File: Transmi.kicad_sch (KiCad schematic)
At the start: 47 parts, among them J101 Bat, J104 Ant, J105 Boot, Q101 Si2301CDS, Q102 XC6220B331MR-G, SW129 SK-3296S-01-L3, U1 ESP32-S2FH4, U103 TP4056, X101 S2240000101050JY, X102 Q13FC1350000400

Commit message: Added LEDs
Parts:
- added C1, C10, C100, C102, C104, C11, C116, C117, C12, C122, C123, C124, C125, C126, C127, C128, C129, C13, C130, C131, C132, C133, C134, C135, C136, C137, C138, C139, C14, C140, C141, C142, C143, C144, C145, C146, C147, C148, C149, C15, C150, C151, C152, C153, C154, C155, C156, C157, C158, C159, C16, C160, C161, C17, C18, C19, C2, C20, C21, C22, C23, C24, C25, C26, C27, C28, C29, C3, C30, C31, C32, C33, C34, C35, C36, C37, C38, C39, C4, C40, C41, C42, C43, C44, C45, C46, C47, C48, C49, C5, C50, C51, C52, C53, C54, C55, C56, C57, C58, C59, C6, C60, C61, C62, C63, C64, C65, C66, C67, C68, C69, C7, C70, C71, C72, C73, C74, C75, C76, C77, C78, C79, C8, C80, C81, C82, C83, C84, C85, C86, C87, C88, C89, C9, C90, C91, C92, C93, C94, C95, C96, C97, C98, C99: 100n, Capacitor_SMD:C_0402_1005Metric, symbol Device:C
- added LED1, LED10, LED100, LED101, LED102, LED103, LED104, LED105, LED106, LED107, LED108, LED109, LED11, LED110, LED111, LED112, LED113, LED114, LED115, LED116, LED117, LED118, LED119, LED12, LED120, LED121, LED122, LED123, LED124, LED125, LED126, LED127, LED128, LED129, LED13, LED130, LED131, LED132, LED133, LED134, LED135, LED136, LED137, LED138, LED139, LED14, LED140, LED141, LED142, LED143, LED144, LED15, LED16, LED17, LED18, LED19, LED2, LED20, LED21, LED22, LED23, LED24, LED25, LED26, LED27, LED28, LED29, LED3, LED30, LED31, LED32, LED33, LED34, LED35, LED36, LED37, LED38, LED39, LED4, LED40, LED41, LED42, LED43, LED44, LED45, LED46, LED47, LED48, LED49, LED5, LED50, LED51, LED52, LED53, LED54, LED55, LED56, LED57, LED58, LED59, LED6, LED60, LED61, LED62, LED63, LED64, LED65, LED66, LED67, LED68, LED69, LED7, LED70, LED71, LED72, LED73, LED74, LED75, LED76, LED77, LED78, LED79, LED8, LED80, LED81, LED82, LED83, LED84, LED85, LED86, LED87, LED88, LED89, LED9, LED90, LED91, LED92, LED93, LED94, LED95, LED96, LED97, LED98, LED99: WS2812B-2020, TransmiLib:LED-SMD_4P-L2.0-W2.0-TL_WS2812B-2020, symbol TransmiLib:WS2812B-2020
- J104: footprint easyeda2kicad:ESPRESSIF_ESP32_MIFA_2.4GHz_Right -> TransmiLib:ESPRESSIF_ESP32_MIFA_2.4GHz_Right
- Q102: footprint easyeda2kicad:SOT-25-5_L3.0-W1.8-P0.95-LS3.0-BR -> TransmiLib:SOT-25_L3.0-W1.6-P0.95-LS2.8-TL; symbol easyeda2kicad:XC6220B331MR-G -> TransmiLib:XC6220B331MR-G
- SW129: footprint easyeda2kicad:SW-SMD_SK-3296S-01-L3 -> TransmiLib:SW-SMD_SK-3296S-01-L3; symbol easyeda2kicad:SK-3296S-01-L3 -> TransmiLib:SK-3296S-01-L3
- U103: footprint easyeda2kicad:ESOP-8_L4.9-W3.9-P1.27-LS6.0-BL-EP -> TransmiLib:ESOP-8_L4.9-W3.9-P1.27-LS6.0-BL-EP; symbol easyeda2kicad:TP4056 -> TransmiLib:TP4056_C725790; LCSC Part C16581 -> C725790
- USB101: footprint easyeda2kicad:USB-C-SMD_TYPE-C16PIN_C668624 -> TransmiLib:USB-C-SMD_TYPE-C16PIN_C668624; symbol easyeda2kicad:TYPE-C16P(073) -> TransmiLib:TYPE-C16P(073)
- X101: footprint easyeda2kicad:CRYSTAL-SMD_4P-L2.5-W2.0-BL -> TransmiLib:CRYSTAL-SMD_4P-L2.5-W2.0-BL; symbol easyeda2kicad:S2240000101050JY -> TransmiLib:S2240000101050; LCSC Part C555614 -> C426970
- X102: footprint easyeda2kicad:FC-135R_L3.2-W1.5 -> TransmiLib:FC-135R_L3.2-W1.5; symbol easyeda2kicad:Q13FC1350000400 -> TransmiLib:Q13FC1350000400
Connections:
- net +5V: now also C1.2, C10.2, C100.2, C102.2, C104.2, C11.2, C116.2, C117.2, C12.2, C122.2, C123.2, C124.2, C125.2, C126.2, C127.2, C128.2, C129.2, C13.2, C130.2, C131.2, C132.2, C133.2, C134.2, C135.2, C136.2, C137.2, C138.2, C139.2, C14.2, C140.2, C141.2, C142.2, C143.2, C144.2, C145.2, C146.2, C147.2, C148.2, C149.2, C15.2, C150.2, C151.2, C152.2, C153.2, C154.2, C155.2, C156.2, C157.2, C158.2, C159.2, C16.2, C160.2, C161.2, C17.2, C18.2, C19.2, C2.2, C20.2, C21.2, C22.2, C23.2, C24.2, C25.2, C26.2, C27.2, C28.2, C29.2, C3.2, C30.2, C31.2, C32.2, C33.2, C34.2, C35.2, C36.2, C37.2, C38.2, C39.2, C4.2, C40.2, C41.2, C42.2, C43.2, C44.2, C45.2, C46.2, C47.2, C48.2, C49.2, C5.2, C50.2, C51.2, C52.2, C53.2, C54.2, C55.2, C56.2, C57.2, C58.2, C59.2, C6.2, C60.2, C61.2, C62.2, C63.2, C64.2, C65.2, C66.2, C67.2, C68.2, C69.2, C7.2, C70.2, C71.2, C72.2, C73.2, C74.2, C75.2, C76.2, C77.2, C78.2, C79.2, C8.2, C80.2, C81.2, C82.2, C83.2, C84.2, C85.2, C86.2, C87.2, C88.2, C89.2, C9.2, C90.2, C91.2, C92.2, C93.2, C94.2, C95.2, C96.2, C97.2, C98.2, C99.2, LED1.4 (VDD), LED10.4 (VDD), LED100.4 (VDD), LED101.4 (VDD), LED102.4 (VDD), LED103.4 (VDD), LED104.4 (VDD), LED105.4 (VDD), LED106.4 (VDD), LED107.4 (VDD), LED108.4 (VDD), LED109.4 (VDD), LED11.4 (VDD), LED110.4 (VDD), LED111.4 (VDD), LED112.4 (VDD), LED113.4 (VDD), LED114.4 (VDD), LED115.4 (VDD), LED116.4 (VDD), LED117.4 (VDD), LED118.4 (VDD), LED119.4 (VDD), LED12.4 (VDD), LED120.4 (VDD), LED121.4 (VDD), LED122.4 (VDD), LED123.4 (VDD), LED124.4 (VDD), LED125.4 (VDD), LED126.4 (VDD), LED127.4 (VDD), LED128.4 (VDD), LED129.4 (VDD), LED13.4 (VDD), LED130.4 (VDD), LED131.4 (VDD), LED132.4 (VDD), LED133.4 (VDD), LED134.4 (VDD), LED135.4 (VDD), LED136.4 (VDD), LED137.4 (VDD), LED138.4 (VDD), LED139.4 (VDD), LED14.4 (VDD), LED140.4 (VDD), LED141.4 (VDD), LED142.4 (VDD), LED143.4 (VDD), LED144.4 (VDD), LED15.4 (VDD), LED16.4 (VDD), LED17.4 (VDD), LED18.4 (VDD), LED19.4 (VDD), LED2.4 (VDD), LED20.4 (VDD), LED21.4 (VDD), LED22.4 (VDD), LED23.4 (VDD), LED24.4 (VDD), LED25.4 (VDD), LED26.4 (VDD), LED27.4 (VDD), LED28.4 (VDD), LED29.4 (VDD), LED3.4 (VDD), LED30.4 (VDD), LED31.4 (VDD), LED32.4 (VDD), LED33.4 (VDD), LED34.4 (VDD), LED35.4 (VDD), LED36.4 (VDD), LED37.4 (VDD), LED38.4 (VDD), LED39.4 (VDD), LED4.4 (VDD), LED40.4 (VDD), LED41.4 (VDD), LED42.4 (VDD), LED43.4 (VDD), LED44.4 (VDD), LED45.4 (VDD), LED46.4 (VDD), LED47.4 (VDD), LED48.4 (VDD), LED49.4 (VDD), LED5.4 (VDD), LED50.4 (VDD), LED51.4 (VDD), LED52.4 (VDD), LED53.4 (VDD), LED54.4 (VDD), LED55.4 (VDD), LED56.4 (VDD), LED57.4 (VDD), LED58.4 (VDD), LED59.4 (VDD), LED6.4 (VDD), LED60.4 (VDD), LED61.4 (VDD), LED62.4 (VDD), LED63.4 (VDD), LED64.4 (VDD), LED65.4 (VDD), LED66.4 (VDD), LED67.4 (VDD), LED68.4 (VDD), LED69.4 (VDD), LED7.4 (VDD), LED70.4 (VDD), LED71.4 (VDD), LED72.4 (VDD), LED73.4 (VDD), LED74.4 (VDD), LED75.4 (VDD), LED76.4 (VDD), LED77.4 (VDD), LED78.4 (VDD), LED79.4 (VDD), LED8.4 (VDD), LED80.4 (VDD), LED81.4 (VDD), LED82.4 (VDD), LED83.4 (VDD), LED84.4 (VDD), LED85.4 (VDD), LED86.4 (VDD), LED87.4 (VDD), LED88.4 (VDD), LED89.4 (VDD), LED9.4 (VDD), LED90.4 (VDD), LED91.4 (VDD), LED92.4 (VDD), LED93.4 (VDD), LED94.4 (VDD), LED95.4 (VDD), LED96.4 (VDD), LED97.4 (VDD), LED98.4 (VDD), LED99.4 (VDD); no longer U103.4 (VCC)
- net +BATT: no longer U103.5 (BAT)
- net Earth: now also C1.1, C10.1, C100.1, C102.1, C104.1, C11.1, C116.1, C117.1, C12.1, C122.1, C123.1, C124.1, C125.1, C126.1, C127.1, C128.1, C129.1, C13.1, C130.1, C131.1, C132.1, C133.1, C134.1, C135.1, C136.1, C137.1, C138.1, C139.1, C14.1, C140.1, C141.1, C142.1, C143.1, C144.1, C145.1, C146.1, C147.1, C148.1, C149.1, C15.1, C150.1, C151.1, C152.1, C153.1, C154.1, C155.1, C156.1, C157.1, C158.1, C159.1, C16.1, C160.1, C161.1, C17.1, C18.1, C19.1, C2.1, C20.1, C21.1, C22.1, C23.1, C24.1, C25.1, C26.1, C27.1, C28.1, C29.1, C3.1, C30.1, C31.1, C32.1, C33.1, C34.1, C35.1, C36.1, C37.1, C38.1, C39.1, C4.1, C40.1, C41.1, C42.1, C43.1, C44.1, C45.1, C46.1, C47.1, C48.1, C49.1, C5.1, C50.1, C51.1, C52.1, C53.1, C54.1, C55.1, C56.1, C57.1, C58.1, C59.1, C6.1, C60.1, C61.1, C62.1, C63.1, C64.1, C65.1, C66.1, C67.1, C68.1, C69.1, C7.1, C70.1, C71.1, C72.1, C73.1, C74.1, C75.1, C76.1, C77.1, C78.1, C79.1, C8.1, C80.1, C81.1, C82.1, C83.1, C84.1, C85.1, C86.1, C87.1, C88.1, C89.1, C9.1, C90.1, C91.1, C92.1, C93.1, C94.1, C95.1, C96.1, C97.1, C98.1, C99.1, LED1.2 (GND), LED10.2 (GND), LED100.2 (GND), LED101.2 (GND), LED102.2 (GND), LED103.2 (GND), LED104.2 (GND), LED105.2 (GND), LED106.2 (GND), LED107.2 (GND), LED108.2 (GND), LED109.2 (GND), LED11.2 (GND), LED110.2 (GND), LED111.2 (GND), LED112.2 (GND), LED113.2 (GND), LED114.2 (GND), LED115.2 (GND), LED116.2 (GND), LED117.2 (GND), LED118.2 (GND), LED119.2 (GND), LED12.2 (GND), LED120.2 (GND), LED121.2 (GND), LED122.2 (GND), LED123.2 (GND), LED124.2 (GND), LED125.2 (GND), LED126.2 (GND), LED127.2 (GND), LED128.2 (GND), LED129.2 (GND), LED13.2 (GND), LED130.2 (GND), LED131.2 (GND), LED132.2 (GND), LED133.2 (GND), LED134.2 (GND), LED135.2 (GND), LED136.2 (GND), LED137.2 (GND), LED138.2 (GND), LED139.2 (GND), LED14.2 (GND), LED140.2 (GND), LED141.2 (GND), LED142.2 (GND), LED143.2 (GND), LED144.2 (GND), LED15.2 (GND), LED16.2 (GND), LED17.2 (GND), LED18.2 (GND), LED19.2 (GND), LED2.2 (GND), LED20.2 (GND), LED21.2 (GND), LED22.2 (GND), LED23.2 (GND), LED24.2 (GND), LED25.2 (GND), LED26.2 (GND), LED27.2 (GND), LED28.2 (GND), LED29.2 (GND), LED3.2 (GND), LED30.2 (GND), LED31.2 (GND), LED32.2 (GND), LED33.2 (GND), LED34.2 (GND), LED35.2 (GND), LED36.2 (GND), LED37.2 (GND), LED38.2 (GND), LED39.2 (GND), LED4.2 (GND), LED40.2 (GND), LED41.2 (GND), LED42.2 (GND), LED43.2 (GND), LED44.2 (GND), LED45.2 (GND), LED46.2 (GND), LED47.2 (GND), LED48.2 (GND), LED49.2 (GND), LED5.2 (GND), LED50.2 (GND), LED51.2 (GND), LED52.2 (GND), LED53.2 (GND), LED54.2 (GND), LED55.2 (GND), LED56.2 (GND), LED57.2 (GND), LED58.2 (GND), LED59.2 (GND), LED6.2 (GND), LED60.2 (GND), LED61.2 (GND), LED62.2 (GND), LED63.2 (GND), LED64.2 (GND), LED65.2 (GND), LED66.2 (GND), LED67.2 (GND), LED68.2 (GND), LED69.2 (GND), LED7.2 (GND), LED70.2 (GND), LED71.2 (GND), LED72.2 (GND), LED73.2 (GND), LED74.2 (GND), LED75.2 (GND), LED76.2 (GND), LED77.2 (GND), LED78.2 (GND), LED79.2 (GND), LED8.2 (GND), LED80.2 (GND), LED81.2 (GND), LED82.2 (GND), LED83.2 (GND), LED84.2 (GND), LED85.2 (GND), LED86.2 (GND), LED87.2 (GND), LED88.2 (GND), LED89.2 (GND), LED9.2 (GND), LED90.2 (GND), LED91.2 (GND), LED92.2 (GND), LED93.2 (GND), LED94.2 (GND), LED95.2 (GND), LED96.2 (GND), LED97.2 (GND), LED98.2 (GND), LED99.2 (GND)
- new net: LED65.3 (DI), LED69.1 (DO)
- new net: LED69.3 (DI), LED73.1 (DO)
- new net: LED1.3 (DI), LED2.1 (DO)
- new net: LED2.3 (DI), LED3.1 (DO)
- new net: LED67.3 (DI), LED71.1 (DO)
- new net: LED71.3 (DI), LED75.1 (DO)
- new net: LED137.3 (DI), LED141.1 (DO)
- new net: LED141.3 (DI), LED98.1 (DO)
- new net: LED12.3 (DI), LED13.1 (DO)
- new net: LED13.3 (DI), LED14.1 (DO)
- new net: LED128.3 (DI), LED132.1 (DO)
- new net: LED132.3 (DI), LED136.1 (DO)
- new net: LED30.3 (DI), LED32.1 (DO)
- new net: LED32.3 (DI), LED34.1 (DO)
- new net: LED55.3 (DI), LED59.1 (DO)
- new net: LED59.3 (DI), LED63.1 (DO)
- new net: LED34.3 (DI), LED36.1 (DO)
- new net: LED136.3 (DI), LED140.1 (DO)
- new net: LED140.3 (DI), LED144.1 (DO)
- new net: LED116.3 (DI), LED120.1 (DO)
- new net: LED120.3 (DI), LED124.1 (DO)
- new net: LED35.3 (DI), LED37.1 (DO)
- new net: LED37.3 (DI), LED39.1 (DO)
- new net: LED89.3 (DI), LED93.1 (DO)
- new net: LED50.1 (DO), LED93.3 (DI)
- new net: LED79.3 (DI), LED83.1 (DO)
- new net: LED83.3 (DI), LED87.1 (DO)
- new net: LED133.3 (DI), LED137.1 (DO)
- new net: LED10.3 (DI), LED11.1 (DO)
- new net: LED11.3 (DI), LED12.1 (DO)
- new net: LED27.3 (DI), LED29.1 (DO)
- new net: LED29.3 (DI), LED31.1 (DO)
- new net: LED21.3 (DI), LED22.1 (DO)
- new net: LED22.3 (DI), LED23.1 (DO)
- new net: LED113.3 (DI), LED117.1 (DO)
- new net: LED117.3 (DI), LED121.1 (DO)
- new net: LED36.3 (DI), LED38.1 (DO)
- new net: LED38.3 (DI), LED40.1 (DO)
- new net: LED124.3 (DI), LED128.1 (DO)
- new net: LED75.3 (DI), LED79.1 (DO)
- new net: LED62.3 (DI), LED66.1 (DO)
- new net: LED66.3 (DI), LED70.1 (DO)
- new net: LED51.3 (DI), LED55.1 (DO)
- new net: LED42.3 (DI), LED44.1 (DO)
- new net: LED44.3 (DI), LED46.1 (DO)
- new net: LED131.3 (DI), LED135.1 (DO)
- new net: LED135.3 (DI), LED139.1 (DO)
- new net: LED102.3 (DI), LED106.1 (DO)
- new net: LED106.3 (DI), LED110.1 (DO)
- new net: LED76.3 (DI), LED80.1 (DO)
- new net: LED80.3 (DI), LED84.1 (DO)
- new net: LED39.3 (DI), LED41.1 (DO)
- new net: LED41.3 (DI), LED43.1 (DO)
- new net: LED112.3 (DI), LED116.1 (DO)
- new net: LED8.3 (DI), LED9.1 (DO)
- new net: LED10.1 (DO), LED9.3 (DI)
- new net: LED77.3 (DI), LED81.1 (DO)
- new net: LED81.3 (DI), LED85.1 (DO)
- new net: LED31.3 (DI), LED33.1 (DO)
- new net: LED17.3 (DI), LED18.1 (DO)
- new net: LED18.3 (DI), LED19.1 (DO)
- new net: LED134.3 (DI), LED138.1 (DO)
- new net: LED138.3 (DI), LED142.1 (DO)
- new net: LED68.3 (DI), LED72.1 (DO)
- new net: LED72.3 (DI), LED76.1 (DO)
- new net: LED96.3 (DI), LED97.1 (DO)
- new net: LED101.1 (DO), LED97.3 (DI)
- new net: LED100.3 (DI), LED104.1 (DO)
- new net: LED104.3 (DI), LED108.1 (DO)
- new net: LED60.3 (DI), LED64.1 (DO)
- new net: LED64.3 (DI), LED68.1 (DO)
- new net: LED25.3 (DI), LED27.1 (DO)
- new net: LED84.3 (DI), LED88.1 (DO)
- new net: LED88.3 (DI), LED92.1 (DO)
- new net: LED109.3 (DI), LED113.1 (DO)
- new net: LED50.3 (DI), LED54.1 (DO)
- new net: LED54.3 (DI), LED58.1 (DO)
- new net: LED110.3 (DI), LED114.1 (DO)
- new net: LED114.3 (DI), LED118.1 (DO)
- new net: LED46.3 (DI), LED48.1 (DO)
- new net: LED48.3 (DI), LED49.1 (DO)
- new net: LED15.3 (DI), LED16.1 (DO)
- new net: LED16.3 (DI), LED17.1 (DO)
- new net: LED51.1 (DO), LED94.3 (DI)
- new net: LED33.3 (DI), LED35.1 (DO)
- new net: LED45.3 (DI), LED47.1 (DO)
- new net: LED26.1 (DO), LED47.3 (DI)
- new net: LED49.3 (DI), LED53.1 (DO)
- new net: LED103.1 (DO), LED99.3 (DI)
- new net: LED103.3 (DI), LED107.1 (DO)
- new net: LED19.3 (DI), LED20.1 (DO)
- new net: LED20.3 (DI), LED21.1 (DO)
- new net: LED123.3 (DI), LED127.1 (DO)
- new net: LED127.3 (DI), LED131.1 (DO)
- new net: LED102.1 (DO), LED98.3 (DI)
- new net: LED105.3 (DI), LED109.1 (DO)
- new net: LED139.3 (DI), LED143.1 (DO)
- new net: LED130.3 (DI), LED134.1 (DO)
- new net: LED119.3 (DI), LED123.1 (DO)
- new net: LED90.3 (DI), LED94.1 (DO)
- new net: LED107.3 (DI), LED111.1 (DO)
- new net: LED52.3 (DI), LED56.1 (DO)
- new net: LED56.3 (DI), LED60.1 (DO)
- new net: LED129.3 (DI), LED133.1 (DO)
- new net: LED122.3 (DI), LED126.1 (DO)
- new net: LED126.3 (DI), LED130.1 (DO)
- new net: LED85.3 (DI), LED89.1 (DO)
- new net: LED53.3 (DI), LED57.1 (DO)
- new net: LED57.3 (DI), LED61.1 (DO)
- new net: LED61.3 (DI), LED65.1 (DO)
- new net: LED26.3 (DI), LED28.1 (DO)
- new net: LED87.3 (DI), LED91.1 (DO)
- new net: LED91.3 (DI), LED95.1 (DO)
- new net: LED73.3 (DI), LED77.1 (DO)
- new net: LED5.3 (DI), LED6.1 (DO)
- new net: LED6.3 (DI), LED7.1 (DO)
- new net: LED40.3 (DI), LED42.1 (DO)
- new net: LED111.3 (DI), LED115.1 (DO)
- new net: LED4.3 (DI), LED5.1 (DO)
- new net: LED115.3 (DI), LED119.1 (DO)
- new net: LED82.3 (DI), LED86.1 (DO)
- new net: LED86.3 (DI), LED90.1 (DO)
- new net: LED92.3 (DI), LED96.1 (DO)
- new net: LED118.3 (DI), LED122.1 (DO)
- new net: LED108.3 (DI), LED112.1 (DO)
- new net: LED100.1 (DO), LED143.3 (DI)
- new net: LED121.3 (DI), LED125.1 (DO)
- new net: LED125.3 (DI), LED129.1 (DO)
- new net: LED43.3 (DI), LED45.1 (DO)
- new net: LED63.3 (DI), LED67.1 (DO)
- new net: LED3.3 (DI), LED4.1 (DO)
- new net: LED74.3 (DI), LED78.1 (DO)
- new net: LED78.3 (DI), LED82.1 (DO)
- new net: LED23.3 (DI), LED24.1 (DO)
- new net: LED24.3 (DI), LED25.1 (DO)
- new net: LED58.3 (DI), LED62.1 (DO)
- new net: LED14.3 (DI), LED15.1 (DO)
- new net: LED28.3 (DI), LED30.1 (DO)
- new net: LED70.3 (DI), LED74.1 (DO)
- new net: LED7.3 (DI), LED8.1 (DO)
- new net: LED101.3 (DI), LED105.1 (DO)
- new net: LED52.1 (DO), LED95.3 (DI)
- new net: LED142.3 (DI), LED99.1 (DO)
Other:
- moved on the sheet: D129, D130, R103, R104, R105

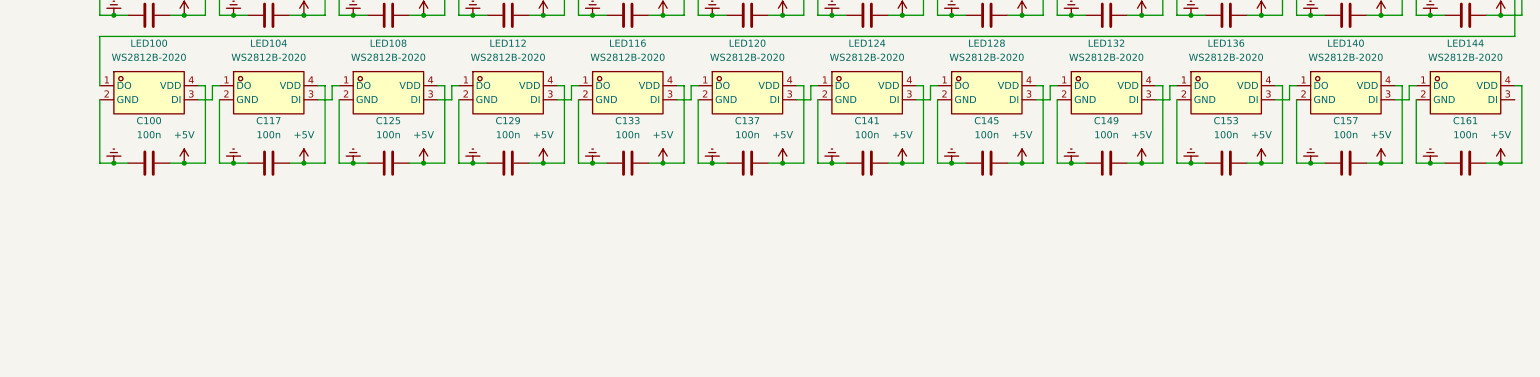
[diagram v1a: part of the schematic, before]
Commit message: Positioned the leds
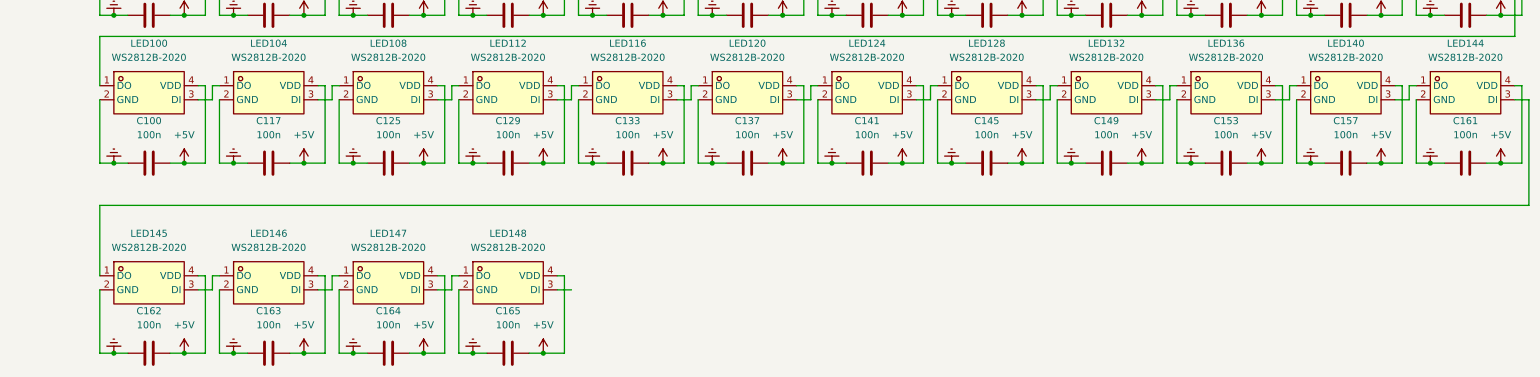
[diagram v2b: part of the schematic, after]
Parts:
- added C162, C163, C164, C165: 100n, Capacitor_SMD:C_0402_1005Metric, symbol Device:C
- added LED145, LED146, LED147, LED148: WS2812B-2020, TransmiLib:LED-SMD_4P-L2.0-W2.0-TL_WS2812B-2020, symbol TransmiLib:WS2812B-2020
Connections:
- net +5V: now also C162.2, C163.2, C164.2, C165.2, LED145.4 (VDD), LED146.4 (VDD), LED147.4 (VDD), LED148.4 (VDD)
- net Earth: now also C162.1, C163.1, C164.1, C165.1, LED145.2 (GND), LED146.2 (GND), LED147.2 (GND), LED148.2 (GND)
- net at LED144.3 (DI): now also LED145.1 (DO)
- new net: LED147.3 (DI), LED148.1 (DO)
- new net: LED146.3 (DI), LED147.1 (DO)
- new net: LED145.3 (DI), LED146.1 (DO)

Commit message: Expensive one
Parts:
- removed C165: 100n, Capacitor_SMD:C_0402_1005Metric, symbol Device:C
- removed LED148: WS2812B-2020, TransmiLib:LED-SMD_4P-L2.0-W2.0-TL_WS2812B-2020, symbol TransmiLib:WS2812B-2020
- added C166: 1000u, Capacitor_THT:CP_Radial_D4.0mm_P2.00mm, symbol Device:C
- added R1: 220, Resistor_SMD:R_0603_1608Metric, symbol Device:R
- renumbered LED6 to LED10, LED137 to LED100, LED57 to LED101, LED98 to LED102, LED129 to LED103, LED114 to LED104, LED102 to LED105, LED74 to LED106, LED62 to LED107, LED92 to LED108, LED39 to LED109, LED70 to LED11, LED27 to LED110, LED15 to LED111, LED136 to LED112, LED58 to LED113, LED101 to LED114, LED130 to LED115, LED115 to LED116, LED103 to LED117, LED73 to LED118, LED75 to LED119, LED88 to LED12, LED93 to LED120, LED38 to LED121, LED26 to LED122, LED147 to LED123, LED135 to LED124, LED59 to LED125, LED118 to LED126, LED131 to LED127, LED133 to LED128, LED104 to LED129, LED47 to LED13, LED72 to LED130, LED61 to LED131, LED94 to LED132, LED37 to LED133, LED25 to LED134, LED146 to LED135, LED48 to LED136, LED60 to LED137, LED119 to LED138, LED132 to LED139, LED35 to LED14, LED134 to LED140, LED105 to LED141, LED71 to LED142, LED96 to LED143, LED95 to LED144, LED116 to LED145, LED117 to LED146, LED84 to LED147, LED83 to LED148, LED23 to LED15, LED144 to LED16, LED50 to LED17, LED77 to LED18, LED121 to LED19, LED36 to LED2, LED107 to LED20, LED3 to LED21, LED8 to LED22, LED69 to LED23, LED87 to LED24, LED46 to LED25, LED34 to LED26, LED22 to LED27, LED143 to LED28, LED51 to LED29, LED24 to LED3, LED78 to LED30, LED122 to LED31, LED108 to LED32, LED2 to LED33, LED9 to LED34, LED68 to LED35, LED86 to LED36, LED45 to LED37, LED33 to LED38, LED21 to LED39, LED145 to LED4, LED142 to LED40, LED52 to LED41, LED79 to LED42, LED123 to LED43, LED109 to LED44, LED1 to LED45, LED10 to LED46, LED67 to LED47, LED85 to LED48, LED44 to LED49, LED49 to LED5, LED32 to LED50, LED20 to LED51, LED141 to LED52, LED80 to LED54, LED125 to LED55, LED110 to LED56, LED4 to LED57, LED11 to LED58, LED66 to LED59, LED76 to LED6, LED124 to LED60, LED43 to LED61, LED31 to LED62, LED19 to LED63, LED140 to LED64, LED54 to LED65, LED81 to LED66, LED126 to LED67, LED111 to LED68, LED5 to LED69, LED120 to LED7, LED12 to LED70, LED65 to LED71, LED89 to LED72, LED42 to LED73, LED30 to LED74, LED18 to LED75, LED139 to LED76, LED55 to LED77, LED82 to LED78, LED127 to LED79, LED106 to LED8, LED112 to LED80, LED99 to LED81, LED13 to LED82, LED64 to LED83, LED90 to LED84, LED41 to LED85, LED29 to LED86, LED17 to LED87, LED138 to LED88, LED56 to LED89, LED7 to LED9, LED97 to LED90, LED128 to LED91, LED113 to LED92, LED100 to LED93, LED14 to LED94, LED63 to LED95, LED91 to LED96, LED40 to LED97, LED28 to LED98, LED16 to LED99
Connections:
- net +5V: no longer C1.2, C10.2, C100.2, C102.2, C104.2, C11.2, C116.2, C117.2, C12.2, C122.2, C123.2, C124.2, C125.2, C126.2, C127.2, C128.2, C129.2, C13.2, C130.2, C131.2, C132.2, C133.2, C134.2, C135.2, C136.2, C137.2, C138.2, C139.2, C14.2, C140.2, C141.2, C142.2, C143.2, C144.2, C145.2, C146.2, C147.2, C148.2, C149.2, C15.2, C150.2, C151.2, C152.2, C153.2, C154.2, C155.2, C156.2, C157.2, C158.2, C159.2, C16.2, C160.2, C161.2, C162.2, C163.2, C164.2, C17.2, C18.2, C19.2, C2.2, C20.2, C21.2, C22.2, C23.2, C24.2, C25.2, C26.2, C27.2, C28.2, C29.2, C3.2, C30.2, C31.2, C32.2, C33.2, C34.2, C35.2, C36.2, C37.2, C38.2, C39.2, C4.2, C40.2, C41.2, C42.2, C43.2, C44.2, C45.2, C46.2, C47.2, C48.2, C49.2, C5.2, C50.2, C51.2, C52.2, C53.2, C54.2, C55.2, C56.2, C57.2, C58.2, C59.2, C6.2, C60.2, C61.2, C62.2, C63.2, C64.2, C65.2, C66.2, C67.2, C68.2, C69.2, C7.2, C70.2, C71.2, C72.2, C73.2, C74.2, C75.2, C76.2, C77.2, C78.2, C79.2, C8.2, C80.2, C81.2, C82.2, C83.2, C84.2, C85.2, C86.2, C87.2, C88.2, C89.2, C9.2, C90.2, C91.2, C92.2, C93.2, C94.2, C95.2, C96.2, C97.2, C98.2, C99.2, LED10.4 (VDD), LED100.4 (VDD), LED101.4 (VDD), LED102.4 (VDD), LED103.4 (VDD), LED104.4 (VDD), LED105.4 (VDD), LED106.4 (VDD), LED107.4 (VDD), LED108.4 (VDD), LED109.4 (VDD), LED11.4 (VDD), LED110.4 (VDD), LED111.4 (VDD), LED112.4 (VDD), LED113.4 (VDD), LED114.4 (VDD), LED115.4 (VDD), LED116.4 (VDD), LED117.4 (VDD), LED118.4 (VDD), LED119.4 (VDD), LED12.4 (VDD), LED120.4 (VDD), LED121.4 (VDD), LED122.4 (VDD), LED123.4 (VDD), LED124.4 (VDD), LED125.4 (VDD), LED126.4 (VDD), LED127.4 (VDD), LED128.4 (VDD), LED129.4 (VDD), LED13.4 (VDD), LED130.4 (VDD), LED131.4 (VDD), LED132.4 (VDD), LED133.4 (VDD), LED134.4 (VDD), LED135.4 (VDD), LED136.4 (VDD), LED137.4 (VDD), LED138.4 (VDD), LED139.4 (VDD), LED14.4 (VDD), LED140.4 (VDD), LED141.4 (VDD), LED142.4 (VDD), LED143.4 (VDD), LED144.4 (VDD), LED145.4 (VDD), LED146.4 (VDD), LED147.4 (VDD), LED148.4 (VDD), LED15.4 (VDD), LED16.4 (VDD), LED17.4 (VDD), LED18.4 (VDD), LED19.4 (VDD), LED2.4 (VDD), LED20.4 (VDD), LED21.4 (VDD), LED22.4 (VDD), LED23.4 (VDD), LED24.4 (VDD), LED25.4 (VDD), LED26.4 (VDD), LED27.4 (VDD), LED28.4 (VDD), LED29.4 (VDD), LED3.4 (VDD), LED30.4 (VDD), LED31.4 (VDD), LED32.4 (VDD), LED33.4 (VDD), LED34.4 (VDD), LED35.4 (VDD), LED36.4 (VDD), LED37.4 (VDD), LED38.4 (VDD), LED39.4 (VDD), LED4.4 (VDD), LED40.4 (VDD), LED41.4 (VDD), LED42.4 (VDD), LED43.4 (VDD), LED44.4 (VDD), LED45.4 (VDD), LED46.4 (VDD), LED47.4 (VDD), LED48.4 (VDD), LED49.4 (VDD), LED5.4 (VDD), LED50.4 (VDD), LED51.4 (VDD), LED52.4 (VDD), LED53.4 (VDD), LED54.4 (VDD), LED55.4 (VDD), LED56.4 (VDD), LED57.4 (VDD), LED58.4 (VDD), LED59.4 (VDD), LED6.4 (VDD), LED60.4 (VDD), LED61.4 (VDD), LED62.4 (VDD), LED63.4 (VDD), LED64.4 (VDD), LED65.4 (VDD), LED66.4 (VDD), LED67.4 (VDD), LED68.4 (VDD), LED69.4 (VDD), LED7.4 (VDD), LED70.4 (VDD), LED71.4 (VDD), LED72.4 (VDD), LED73.4 (VDD), LED74.4 (VDD), LED75.4 (VDD), LED76.4 (VDD), LED77.4 (VDD), LED78.4 (VDD), LED79.4 (VDD), LED8.4 (VDD), LED80.4 (VDD), LED81.4 (VDD), LED82.4 (VDD), LED83.4 (VDD), LED84.4 (VDD), LED85.4 (VDD), LED86.4 (VDD), LED87.4 (VDD), LED88.4 (VDD), LED89.4 (VDD), LED9.4 (VDD), LED90.4 (VDD), LED91.4 (VDD), LED92.4 (VDD), LED93.4 (VDD), LED94.4 (VDD), LED95.4 (VDD), LED96.4 (VDD), LED97.4 (VDD), LED98.4 (VDD), LED99.4 (VDD)
- net Earth: now also C166.2
- net VCC: now also C1.2, C10.2, C100.2, C102.2, C104.2, C11.2, C116.2, C117.2, C12.2, C122.2, C123.2, C124.2, C125.2, C126.2, C127.2, C128.2, C129.2, C13.2, C130.2, C131.2, C132.2, C133.2, C134.2, C135.2, C136.2, C137.2, C138.2, C139.2, C14.2, C140.2, C141.2, C142.2, C143.2, C144.2, C145.2, C146.2, C147.2, C148.2, C149.2, C15.2, C150.2, C151.2, C152.2, C153.2, C154.2, C155.2, C156.2, C157.2, C158.2, C159.2, C16.2, C160.2, C161.2, C162.2, C163.2, C164.2, C17.2, C18.2, C19.2, C2.2, C20.2, C21.2, C22.2, C23.2, C24.2, C25.2, C26.2, C27.2, C28.2, C29.2, C3.2, C30.2, C31.2, C32.2, C33.2, C34.2, C35.2, C36.2, C37.2, C38.2, C39.2, C4.2, C40.2, C41.2, C42.2, C43.2, C44.2, C45.2, C46.2, C47.2, C48.2, C49.2, C5.2, C50.2, C51.2, C52.2, C53.2, C54.2, C55.2, C56.2, C57.2, C58.2, C59.2, C6.2, C60.2, C61.2, C62.2, C63.2, C64.2, C65.2, C66.2, C67.2, C68.2, C69.2, C7.2, C70.2, C71.2, C72.2, C73.2, C74.2, C75.2, C76.2, C77.2, C78.2, C79.2, C8.2, C80.2, C81.2, C82.2, C83.2, C84.2, C85.2, C86.2, C87.2, C88.2, C89.2, C9.2, C90.2, C91.2, C92.2, C93.2, C94.2, C95.2, C96.2, C97.2, C98.2, C99.2, LED10.4 (VDD), LED100.4 (VDD), LED101.4 (VDD), LED102.4 (VDD), LED103.4 (VDD), LED104.4 (VDD), LED105.4 (VDD), LED106.4 (VDD), LED107.4 (VDD), LED108.4 (VDD), LED109.4 (VDD), LED11.4 (VDD), LED110.4 (VDD), LED111.4 (VDD), LED112.4 (VDD), LED113.4 (VDD), LED114.4 (VDD), LED115.4 (VDD), LED116.4 (VDD), LED117.4 (VDD), LED118.4 (VDD), LED119.4 (VDD), LED12.4 (VDD), LED120.4 (VDD), LED121.4 (VDD), LED122.4 (VDD), LED123.4 (VDD), LED124.4 (VDD), LED125.4 (VDD), LED126.4 (VDD), LED127.4 (VDD), LED128.4 (VDD), LED129.4 (VDD), LED13.4 (VDD), LED130.4 (VDD), LED131.4 (VDD), LED132.4 (VDD), LED133.4 (VDD), LED134.4 (VDD), LED135.4 (VDD), LED136.4 (VDD), LED137.4 (VDD), LED138.4 (VDD), LED139.4 (VDD), LED14.4 (VDD), LED140.4 (VDD), LED141.4 (VDD), LED142.4 (VDD), LED143.4 (VDD), LED144.4 (VDD), LED145.4 (VDD), LED146.4 (VDD), LED147.4 (VDD), LED148.4 (VDD), LED15.4 (VDD), LED16.4 (VDD), LED17.4 (VDD), LED18.4 (VDD), LED19.4 (VDD), LED2.4 (VDD), LED20.4 (VDD), LED21.4 (VDD), LED22.4 (VDD), LED23.4 (VDD), LED24.4 (VDD), LED25.4 (VDD), LED26.4 (VDD), LED27.4 (VDD), LED28.4 (VDD), LED29.4 (VDD), LED3.4 (VDD), LED30.4 (VDD), LED31.4 (VDD), LED32.4 (VDD), LED33.4 (VDD), LED34.4 (VDD), LED35.4 (VDD), LED36.4 (VDD), LED37.4 (VDD), LED38.4 (VDD), LED39.4 (VDD), LED4.4 (VDD), LED40.4 (VDD), LED41.4 (VDD), LED42.4 (VDD), LED43.4 (VDD), LED44.4 (VDD), LED45.4 (VDD), LED46.4 (VDD), LED47.4 (VDD), LED48.4 (VDD), LED49.4 (VDD), LED5.4 (VDD), LED50.4 (VDD), LED51.4 (VDD), LED52.4 (VDD), LED53.4 (VDD), LED54.4 (VDD), LED55.4 (VDD), LED56.4 (VDD), LED57.4 (VDD), LED58.4 (VDD), LED59.4 (VDD), LED6.4 (VDD), LED60.4 (VDD), LED61.4 (VDD), LED62.4 (VDD), LED63.4 (VDD), LED64.4 (VDD), LED65.4 (VDD), LED66.4 (VDD), LED67.4 (VDD), LED68.4 (VDD), LED69.4 (VDD), LED7.4 (VDD), LED70.4 (VDD), LED71.4 (VDD), LED72.4 (VDD), LED73.4 (VDD), LED74.4 (VDD), LED75.4 (VDD), LED76.4 (VDD), LED77.4 (VDD), LED78.4 (VDD), LED79.4 (VDD), LED8.4 (VDD), LED80.4 (VDD), LED81.4 (VDD), LED82.4 (VDD), LED83.4 (VDD), LED84.4 (VDD), LED85.4 (VDD), LED86.4 (VDD), LED87.4 (VDD), LED88.4 (VDD), LED89.4 (VDD), LED9.4 (VDD), LED90.4 (VDD), LED91.4 (VDD), LED92.4 (VDD), LED93.4 (VDD), LED94.4 (VDD), LED95.4 (VDD), LED96.4 (VDD), LED97.4 (VDD), LED98.4 (VDD), LED99.4 (VDD), C166.1
- net LED: now reaches LED123.3 (DI)
- net LED: now also R1.2
- net at U1.37 (GPIO33): now also R1.1
- no-connect marks 46 -> 45
